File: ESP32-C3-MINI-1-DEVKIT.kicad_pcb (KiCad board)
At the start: 2 copper layers, 31 parts, among them J1 USB_C_Receptacle_USB2.0, Q1 MMSS8050, Q2 MMSS8050, SW1 TL6330AF200Q, SW2 TL6330AF200Q, U1 ESP32-C3-MINI-1, U2 MCP1825S, U3 CP2102N-Axx-xQFN24

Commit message: layout continues
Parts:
- moved D2 92.8 mm to (188.0, 36.2), turned to 180 degrees
- moved D5 74.4 mm to (165.9, 51.2), turned to 180 degrees
- moved D4 73.0 mm to (165.9, 53.3), turned to 180 degrees
- moved C4 67.5 mm to (180.1, 33.8), turned to 180 degrees
- moved C5 66.8 mm to (180.1, 36.0), turned to 180 degrees
- moved C6 60.5 mm to (195.5, 64.3), turned to 90 degrees
- moved C1 57.7 mm to (171.9, 28.6), turned to 90 degrees
- moved SW1 56.4 mm to (192.5, 63.2), turned to 90 degrees
- moved Q2 49.9 mm to (168.4, 59.2), turned to 180 degrees
- moved Q1 49.8 mm to (168.4, 62.9), turned to 180 degrees
- moved C3 49.0 mm to (193.9, 49.6), turned to -90 degrees
- moved R11 42.6 mm to (171.6, 61.2), turned to 90 degrees
- moved R6 42.1 mm to (188.2, 38.3)
- moved R10 39.8 mm to (168.4, 65.9)
- moved C2 39.0 mm to (180.0, 40.5), turned to 180 degrees
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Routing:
- net USB_GND: track 17.8 -> 41.9 mm, vias 10 -> 16
- net 3V3_BUS: track 0.00 -> 15.7 mm
- net CP2102_DTR: track 0.00 -> 12.7 mm, vias 0 -> 2
- net 5V_USB: track 3.07 -> 15.1 mm
- net /CHIP_PU: track 5.39 -> 11.3 mm
- net Net-(Q2-Pad1): track 0.00 -> 2.23 mm
- net Net-(D2-Pad2): track 0.00 -> 2.14 mm
- net Net-(Q1-Pad1): track 0.00 -> 2.08 mm
- net CP2102_RTS: track 0.00 -> 2.06 mm
- net Net-(D5-Pad2): track 0.00 -> 1.83 mm
- net Net-(D4-Pad2): track 0.00 -> 1.83 mm
- net Net-(D1-Pad2): track 0.00 -> 1.76 mm
- net USB_D-: track 21.5 -> 22.2 mm
- net USB_D+: track 19.2 -> 19.8 mm
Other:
- board outline added: 23 x 66 mm

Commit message: layout progress
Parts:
- added J2: MINI_OUTS_1, Connector_PinHeader_2.54mm:PinHeader_1x06_P2.54mm_Vertical, F.Cu at (133.1, 75.5)
- added J3: CP2102_OUTPUTS, Connector_PinHeader_2.54mm:PinHeader_1x02_P2.54mm_Vertical, F.Cu at (133.1, 93.3)
- added J4: MINI_OUTS_2, Connector_PinHeader_2.54mm:PinHeader_1x06_P2.54mm_Vertical, F.Cu at (156.1, 88.2)
- added J5: PWR_OUTPUTS, Connector_PinHeader_2.54mm:PinHeader_1x04_P2.54mm_Vertical, F.Cu at (156.3, 111.1)
- moved SW1 77.4 mm to (152.6, 129.6)
- moved U1 76.7 mm to (144.8, 74.6)
- moved D3 75.7 mm to (150.5, 111.1)
- moved U2 75.7 mm to (149.7, 117.3)
- moved C4 75.6 mm to (147.9, 102.2), turned to 0 degrees
- moved R6 75.1 mm to (152.6, 104.4)
- moved D1 75.1 mm to (139.7, 112.9)
- moved D2 75.1 mm to (152.4, 102.3)
- moved J1 75.1 mm to (144.4, 129.7)
- moved R2 75.1 mm to (152.6, 106.8)
- moved U3 75.1 mm to (139.6, 119.0)
- moved R5 75.0 mm to (139.0, 122.9)
- moved C2 74.8 mm to (144.6, 106.4), turned to 0 degrees
- moved C6 74.6 mm to (152.6, 125.3), turned to 180 degrees
- moved R3 73.2 mm to (138.9, 107.1)
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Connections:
- net Net-(D3-Pad2) renamed /VBUS_5V
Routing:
- net 3V3_BUS: track 15.7 -> 78.1 mm, vias 0 -> 8
- net /CHIP_PU: track 11.3 -> 33.9 mm, vias 0 -> 2
- net USB_GND: track 41.9 -> 63.8 mm, vias 16 -> 35
- net 5V_USB: track 15.1 -> 36.1 mm, vias 0 -> 4
- net /VBUS_5V: track 30.9 -> 51.9 mm
- net /GPIO2: track 0.00 -> 19.4 mm
- net /GPIO5: track 0.00 -> 17.5 mm
- net /GPIO10: track 0.00 -> 15.7 mm, vias 0 -> 1
- net /GPIO6: track 0.00 -> 14.7 mm
- net /GPIO4: track 0.00 -> 14.5 mm
- net /GPIO3: track 0.00 -> 12.7 mm, vias 0 -> 1
- net /GPIO7: track 0.00 -> 11.7 mm
- net Net-(D1-Pad2): track 1.76 -> 13.3 mm
- net /GPIO1: track 0.00 -> 11.4 mm
- net /GPIO0: track 0.00 -> 11.1 mm
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- added copper zone on B.Cu, net USB_GND
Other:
- board size 23 x 66 mm -> 27.3 x 70 mm

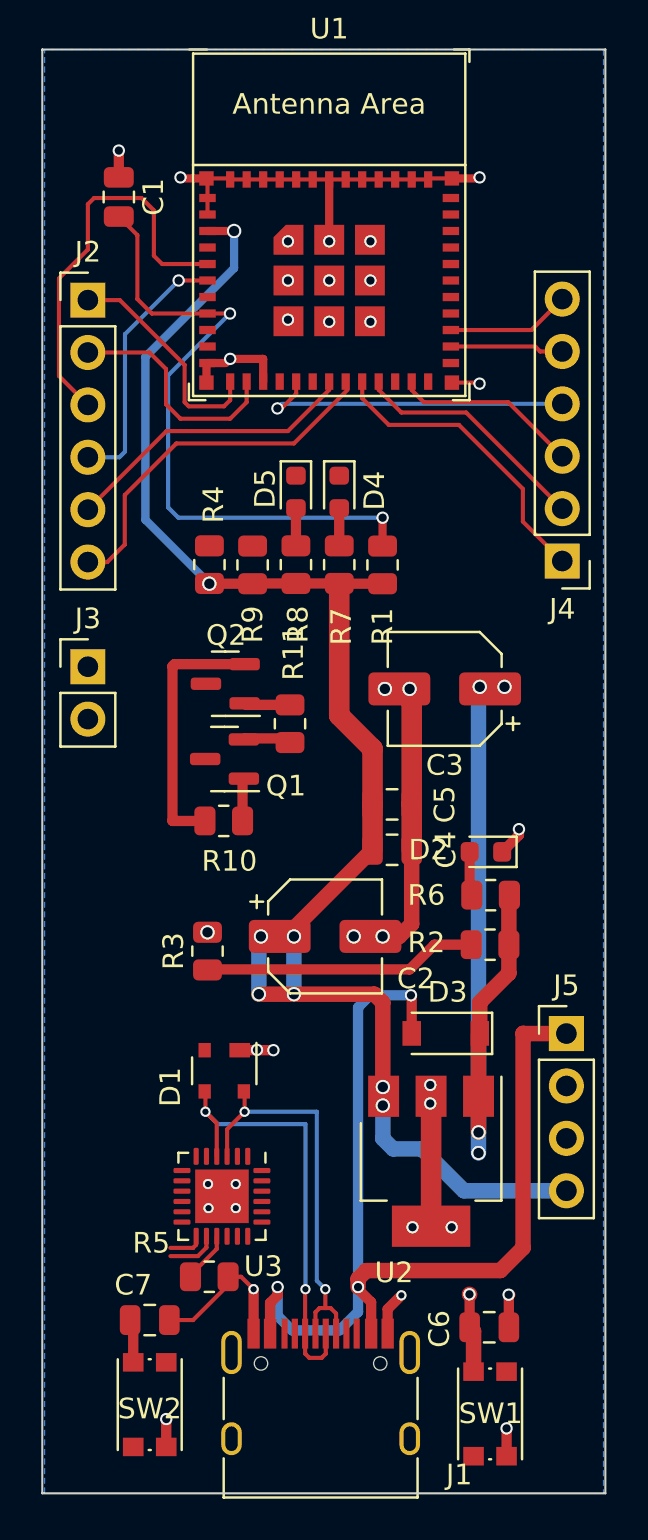
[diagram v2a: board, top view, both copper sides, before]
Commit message: layout finished, does not pass DRC
need to revise and pass DRC now
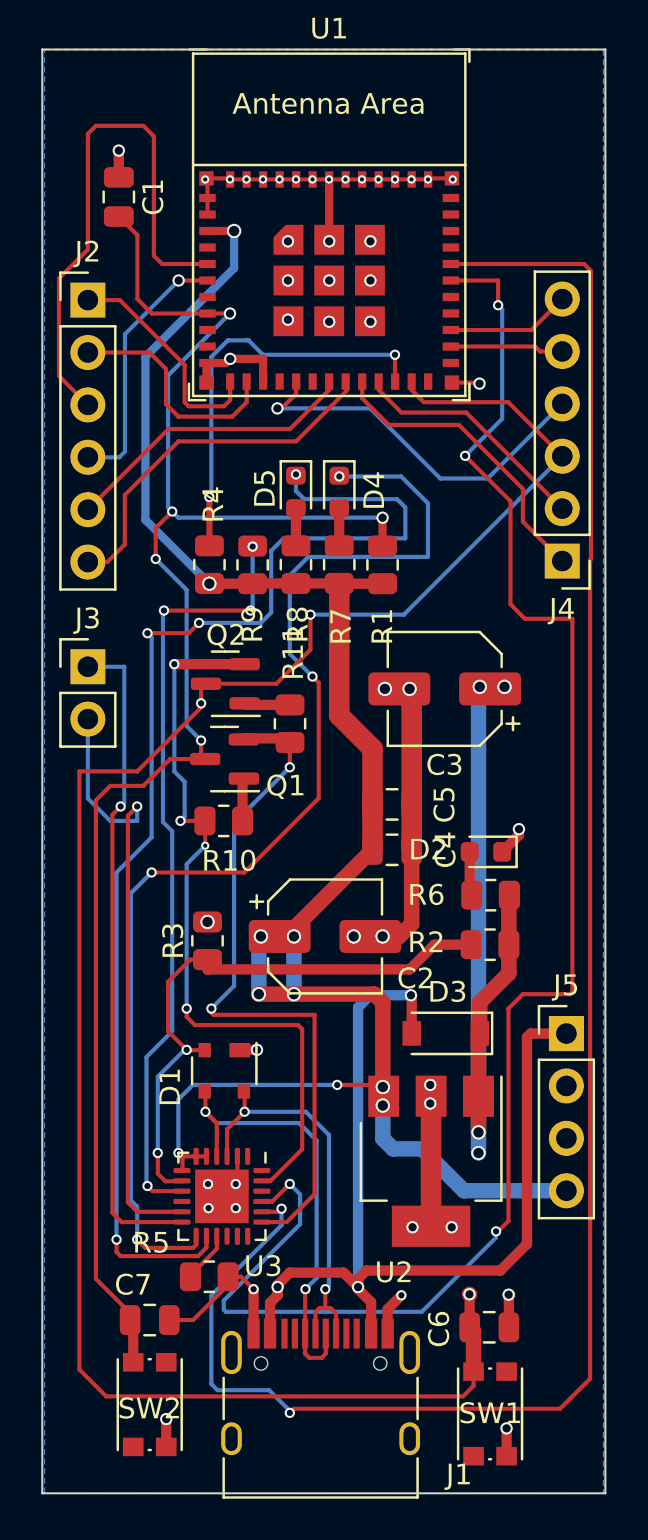
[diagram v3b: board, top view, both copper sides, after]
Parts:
- moved R3 0.50 mm to (138.9, 106.6)
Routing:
- net CP2102_RXD: track 0.00 -> 91.3 mm, vias 0 -> 2
- net /GPIO9: track 12.9 -> 93.7 mm, vias 1 -> 3
- net CP2102_TXD: track 0.00 -> 80.2 mm, vias 0 -> 4
- net /GPIO.0: track 2.47 -> 60.0 mm, vias 0 -> 4
- net /GPIO.1: track 1.73 -> 57.3 mm, vias 0 -> 4
- net /CHIP_PU: track 33.9 -> 79.2 mm, vias 2 -> 5
- net Net-(R9-Pad2): track 0.00 -> 37.9 mm, vias 0 -> 4
- net /GPIO.2: track 0.00 -> 32.0 mm, vias 0 -> 1
- net CP2102_RTS: track 2.06 -> 33.6 mm, vias 0 -> 2
- net /GPIO.3: track 0.00 -> 29.6 mm, vias 0 -> 1
- net CP2102_DTR: track 12.6 -> 36.8 mm, vias 0 -> 4
- net Net-(R4-Pad2): track 0.00 -> 20.0 mm, vias 0 -> 2
- net 3V3_BUS: track 78.1 -> 93.5 mm, vias 8 -> 10
- net Net-(D1-Pad2): track 13.3 -> 28.2 mm, vias 0 -> 2
- net /GPIO2: track 19.4 -> 26.4 mm
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
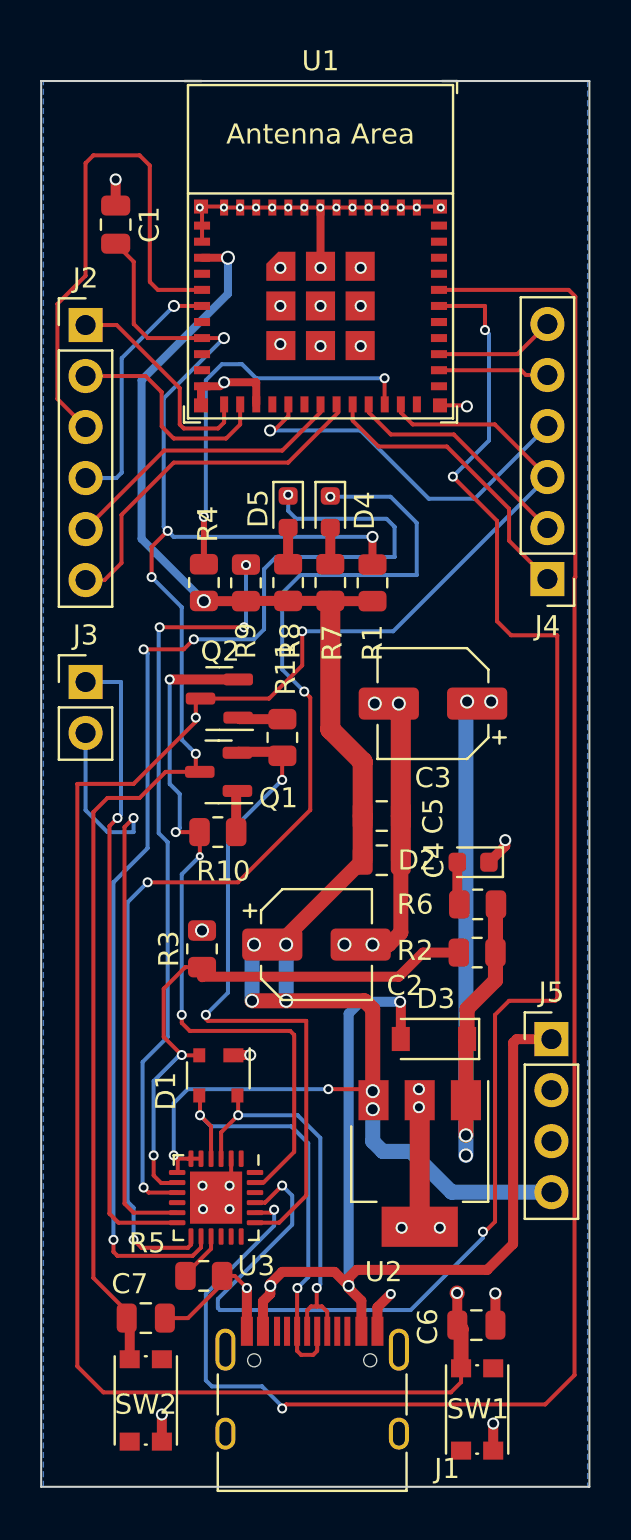
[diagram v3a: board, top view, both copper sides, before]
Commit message: passes DRC
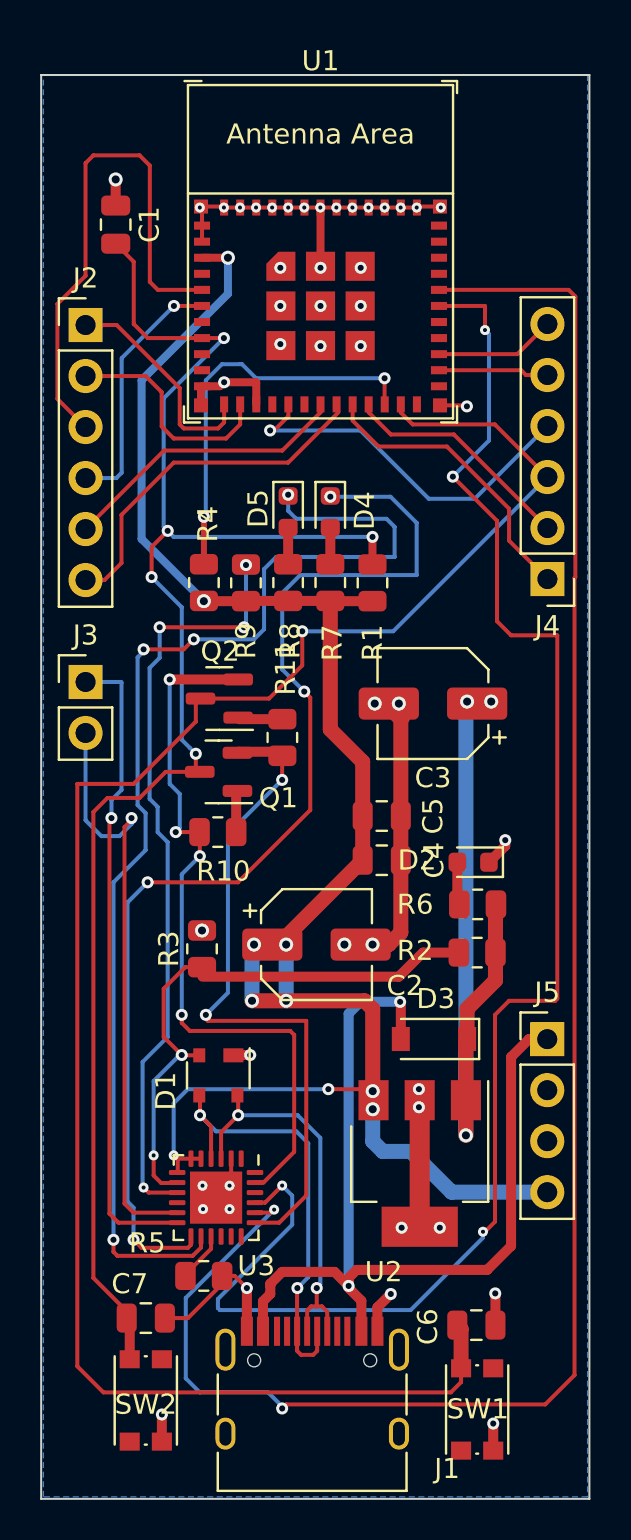
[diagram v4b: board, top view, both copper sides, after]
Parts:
- moved J5 0.21 mm to (156.1, 111.1)
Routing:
- net /GPIO9: track 93.7 -> 92.1 mm, vias 3 -> 1
- net 5V_USB: track 36.1 -> 34.7 mm, vias 4 -> 3
- net CP2102_RXD: track 91.3 -> 92.6 mm
- net /VBUS_5V: track 49.0 -> 48.6 mm, vias 3 -> 2
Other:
- board size 27.3 x 70 mm -> 27.3 x 70.9 mm

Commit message: silkscreen done
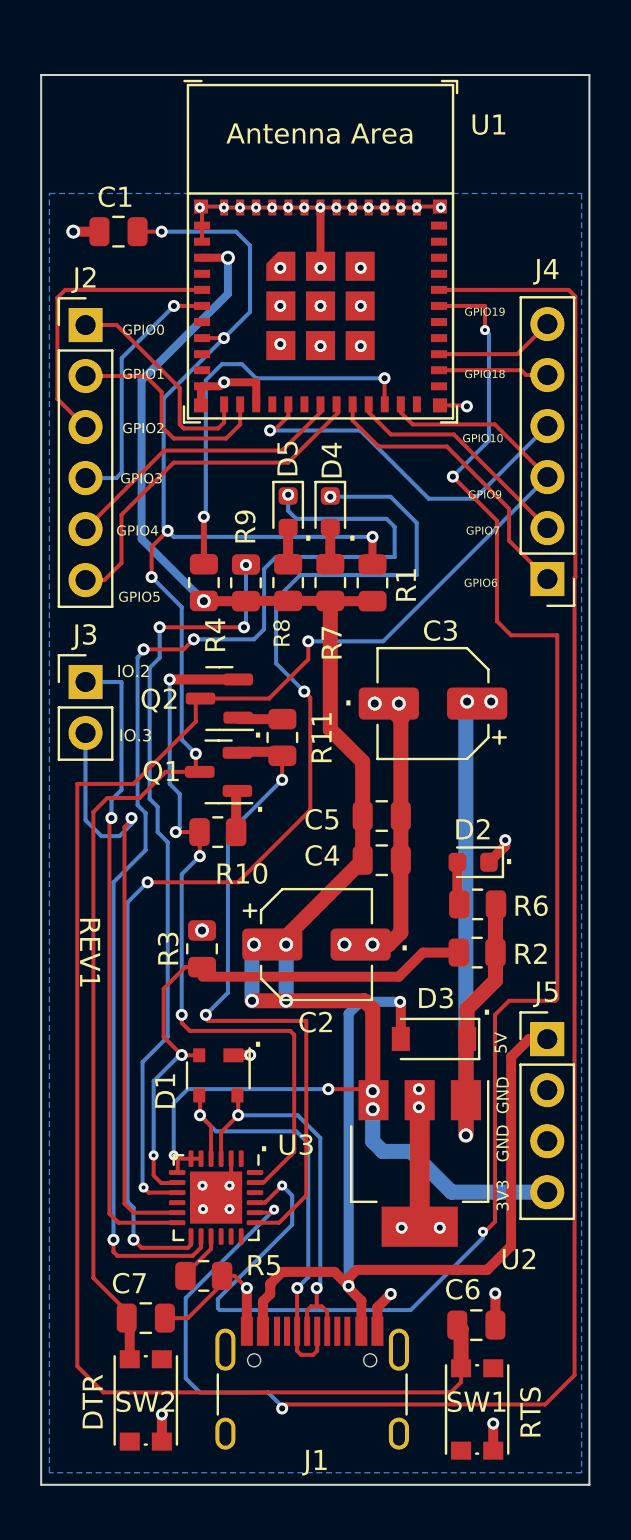
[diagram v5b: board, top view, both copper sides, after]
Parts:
- moved C1 0.38 mm to (134.8, 70.9), turned to 0 degrees
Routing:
- net /GPIO2: track 26.4 -> 14.4 mm
- net /CHIP_PU: track 79.2 -> 82.2 mm, vias 5 -> 6
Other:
- board size 27.3 x 70.9 mm -> 27.3 x 70.2 mm
- board text added: "."
- board text added: "3V3"
- board text added: "5V"
- board text added: "DTR"
- board text added: "GND"
- board text added: "GPIO0"
- board text added: "GPIO1"
- board text added: "GPIO10"
- board text added: "GPIO18"
- board text added: "GPIO19"
- board text added: "GPIO2"
- board text added: "GPIO3"
- board text added: "GPIO4"
- board text added: "GPIO5"
- board text added: "GPIO6"
- board text added: "GPIO7"
- board text added: "GPIO9"
- board text added: "IO.2"
- board text added: "IO.3"
- board text added: "REV1"
- board text added: "RTS"
